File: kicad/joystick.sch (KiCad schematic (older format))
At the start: 16 parts, among them U13 74AHC541, U14 74AHC541

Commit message: Update to Kicad 5
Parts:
- C8, C9: symbol C -> Device:C
- JOY1, JOY2: symbol DB9_Male_MountingHoles -> Connector:DB9_Male_MountingHoles
- R10, R11, R2, R3, R4, R5, R6, R7, R8, R9: symbol R -> Device:R
- U13, U14: symbol 74LS541 -> 74xx:74LS541
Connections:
- wire segments 82 -> 102

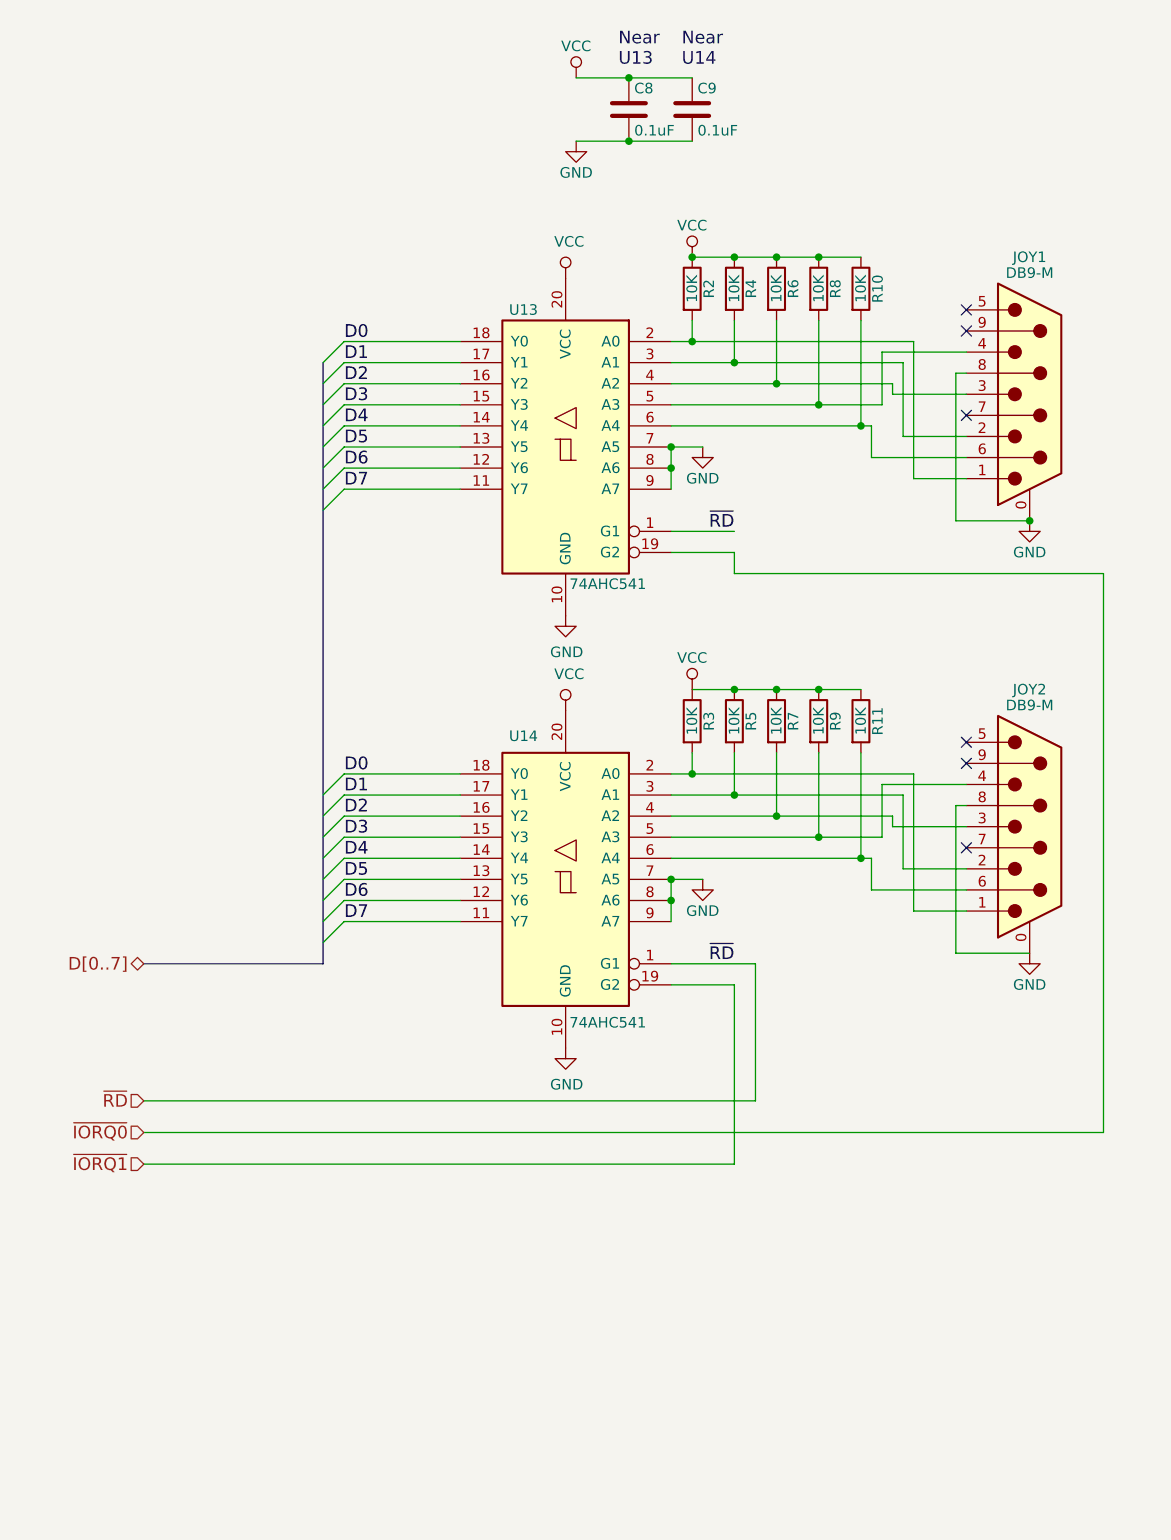
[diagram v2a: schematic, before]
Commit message: Hook up SD card slot's write protect and card detect lines.
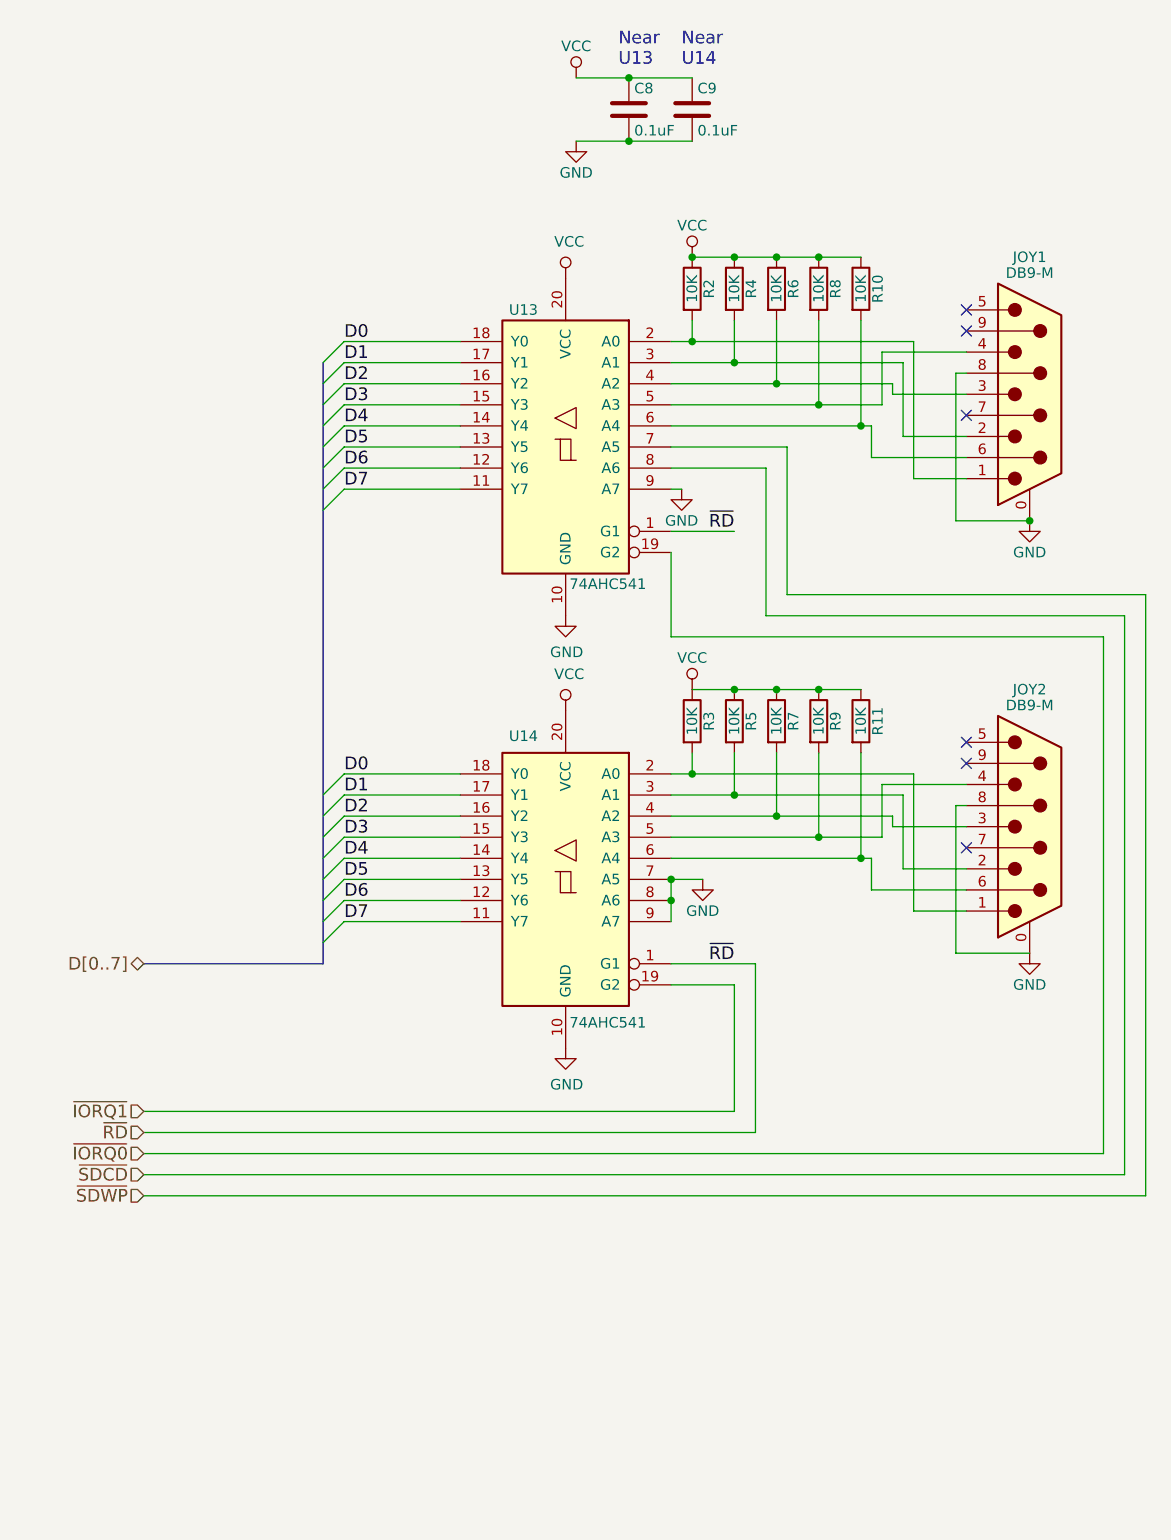
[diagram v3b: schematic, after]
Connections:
- net GND: no longer U13.7 (A5), U13.8 (A6)
- new net ~SDCD: U13.8 (A6)
- new net ~SDWP: U13.7 (A5)
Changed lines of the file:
@@
 Wire Wire Line
 	6250 2550 6250 2050
-Wire Wire Line
-	5350 3150 5650 3150
 $Comp
 L power:GND #PWR026
 U 1 1 59D6AB23
-P 5500 2650
-F 0 "#PWR026" H 5500 2400 50  0001 C CNN
-F 1 "GND" H 5500 2500 50  0000 C CNN
-F 2 "" H 5500 2650 50  0001 C CNN
-F 3 "" H 5500 2650 50  0001 C CNN
-	1    5500 2650
-	1    0    0    -1
-$EndComp
-Wire Wire Line
-	5350 2650 5500 2650
+P 5400 2850
+F 0 "#PWR026" H 5400 2600 50  0001 C CNN
+F 1 "GND" H 5400 2700 50  0000 C CNN
+F 2 "" H 5400 2850 50  0001 C CNN
+F 3 "" H 5400 2850 50  0001 C CNN
+	1    5400 2850
+	1    0    0    -1
+$EndComp
 Wire Wire Line
 	6750 2800 6500 2800
@@
 Text HLabel 2850 5100 0    60   BiDi ~ 0
 D[0..7]
-Text HLabel 2850 5750 0    60   Input ~ 0
+Text HLabel 2850 5900 0    60   Input ~ 0
 ~RD
 Wire Wire Line
-	2850 5750 5750 5750
-Text HLabel 2850 5900 0    60   Input ~ 0
+	2850 5900 5750 5900
+Text HLabel 2850 6000 0    60   Input ~ 0
 ~IORQ0
-Text HLabel 2850 6050 0    60   Input ~ 0
+Text HLabel 2850 5800 0    60   Input ~ 0
 ~IORQ1
 Wire Wire Line
-	5650 6050 2850 6050
-Wire Wire Line
-	2850 5900 7400 5900
-Wire Wire Line
-	7400 3250 5650 3250
-Wire Wire Line
-	5650 3250 5650 3150
+	5650 5800 2850 5800
 Wire Bus Line
 	3700 5100 2850 5100
@@
 	5150 1200 5450 1200
 Wire Wire Line
-	5350 2850 5350 2750
-Wire Wire Line
-	5350 2750 5350 2650
-Connection ~ 5350 2750
-Connection ~ 5350 2650
-Wire Wire Line
 	5350 4900 5350 4800
 Wire Wire Line
@@
 $EndComp
 Wire Wire Line
-	5750 5100 5750 5750
-Wire Wire Line
-	5650 5200 5650 6050
+	5750 5100 5750 5900
+Wire Wire Line
+	5650 5200 5650 5800
 Connection ~ 5450 1750
 Connection ~ 7050 3000
@@
 $EndComp
 Wire Wire Line
-	7400 3250 7400 5900
+	5400 2850 5350 2850
+Wire Wire Line
+	2850 6000 7400 6000
+Wire Wire Line
+	5350 3150 5350 3550
+Wire Wire Line
+	5350 3550 7400 3550
+Wire Wire Line
+	7400 3550 7400 6000
+Wire Wire Line
+	5350 2750 5800 2750
+Wire Wire Line
+	5800 2750 5800 3450
+Wire Wire Line
+	5800 3450 7500 3450
+Wire Wire Line
+	7500 3450 7500 6100
+Wire Wire Line
+	7500 6100 2850 6100
+Wire Wire Line
+	5350 2650 5900 2650
+Wire Wire Line
+	5900 2650 5900 3350
+Wire Wire Line
+	5900 3350 7600 3350
+Wire Wire Line
+	7600 3350 7600 6200
+Wire Wire Line
+	7600 6200 2850 6200
 Wire Bus Line
 	3700 2250 3700 5100
+Text HLabel 2850 6100 0    60   Input ~ 0
+~SDCD
+Text HLabel 2850 6200 0    60   Input ~ 0
+~SDWP
 $EndSCHEMATC

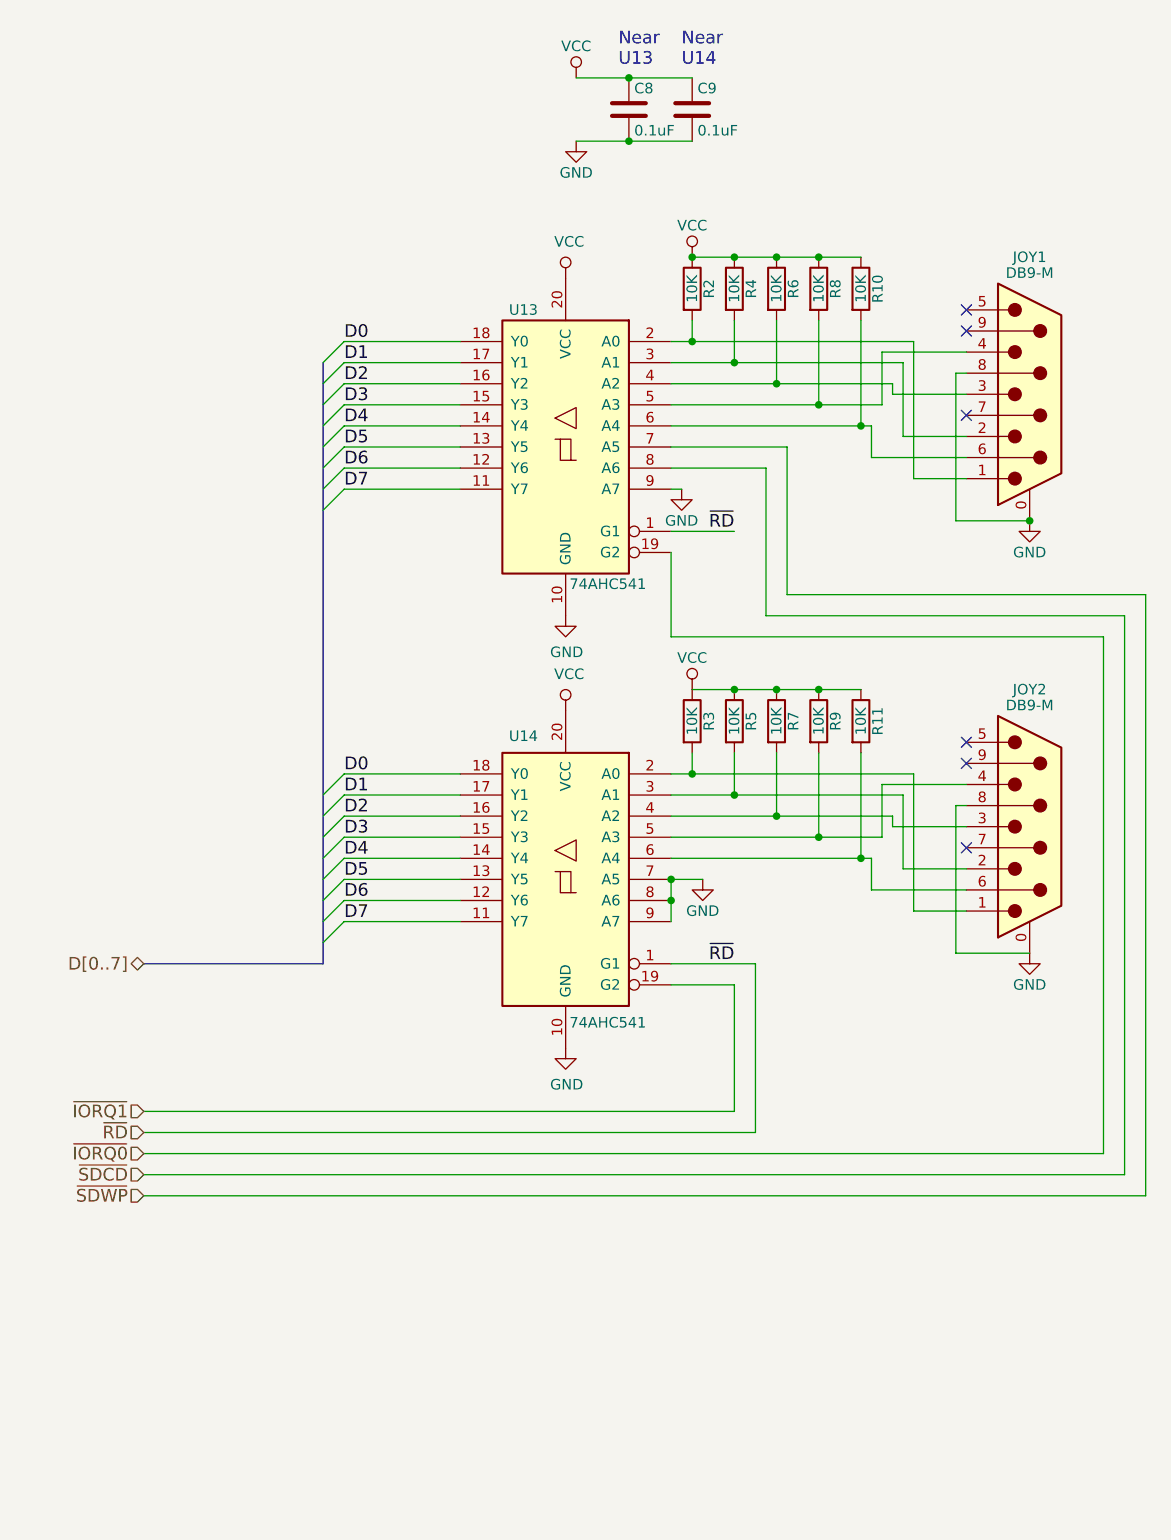
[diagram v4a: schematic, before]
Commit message: First complete version of ZED-80 schematic.
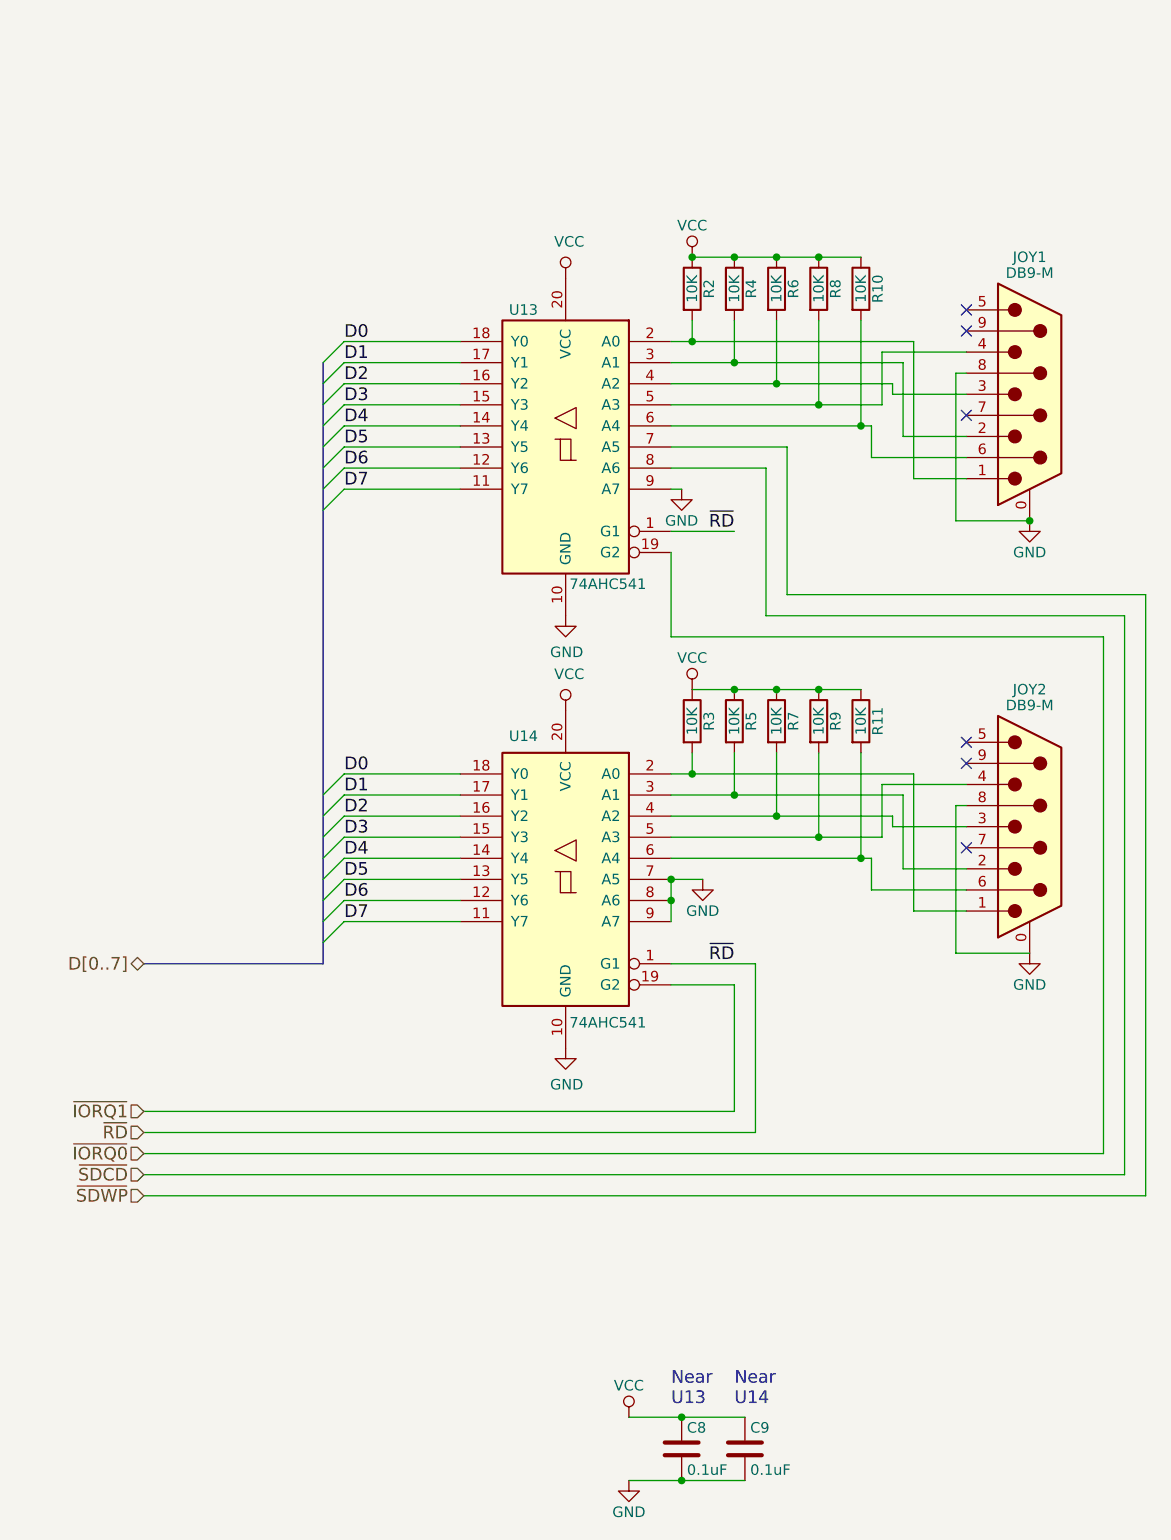
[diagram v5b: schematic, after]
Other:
- moved on the sheet: C8, C9
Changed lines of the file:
@@
 EESchema Schematic File Version 4
-LIBS:z80-cache
 EELAYER 29 0
 EELAYER END
@@
 Sheet 2 11
 Title "Joystick Ports"
-Date "2018-07-20"
-Rev "12"
+Date "2019-04-03"
+Rev "1"
 Comp ""
 Comment1 ""
@@
 L Device:C C8
 U 1 1 59D817E3
-P 5150 1050
-F 0 "C8" H 5175 1150 50  0000 L CNN
-F 1 "0.1uF" H 5175 950 50  0000 L CNN
-F 2 "Capacitors_THT:C_Disc_D4.3mm_W1.9mm_P5.00mm" H 5188 900 50  0001 C CNN
-F 3 "" H 5150 1050 50  0001 C CNN
-	1    5150 1050
+P 5400 7400
+F 0 "C8" H 5425 7500 50  0000 L CNN
+F 1 "0.1uF" H 5425 7300 50  0000 L CNN
+F 2 "Capacitors_THT:C_Disc_D4.3mm_W1.9mm_P5.00mm" H 5438 7250 50  0001 C CNN
+F 3 "" H 5400 7400 50  0001 C CNN
+	1    5400 7400
 	1    0    0    -1
 $EndComp
@@
 L power:GND #PWR030
 U 1 1 59D817EA
-P 4900 1200
-F 0 "#PWR030" H 4900 950 50  0001 C CNN
-F 1 "GND" H 4900 1050 50  0000 C CNN
-F 2 "" H 4900 1200 50  0001 C CNN
-F 3 "" H 4900 1200 50  0001 C CNN
-	1    4900 1200
+P 5150 7550
+F 0 "#PWR030" H 5150 7300 50  0001 C CNN
+F 1 "GND" H 5150 7400 50  0000 C CNN
+F 2 "" H 5150 7550 50  0001 C CNN
+F 3 "" H 5150 7550 50  0001 C CNN
+	1    5150 7550
 	1    0    0    -1
 $EndComp
@@
 L Device:C C9
 U 1 1 59D817F0
-P 5450 1050
-F 0 "C9" H 5475 1150 50  0000 L CNN
-F 1 "0.1uF" H 5475 950 50  0000 L CNN
-F 2 "Capacitors_THT:C_Disc_D4.3mm_W1.9mm_P5.00mm" H 5488 900 50  0001 C CNN
-F 3 "" H 5450 1050 50  0001 C CNN
-	1    5450 1050
+P 5700 7400
+F 0 "C9" H 5725 7500 50  0000 L CNN
+F 1 "0.1uF" H 5725 7300 50  0000 L CNN
+F 2 "Capacitors_THT:C_Disc_D4.3mm_W1.9mm_P5.00mm" H 5738 7250 50  0001 C CNN
+F 3 "" H 5700 7400 50  0001 C CNN
+	1    5700 7400
 	1    0    0    -1
 $EndComp
@@
 L power:VCC #PWR031
 U 1 1 59D817F7
-P 4900 900
-F 0 "#PWR031" H 4900 750 50  0001 C CNN
-F 1 "VCC" H 4900 1050 50  0000 C CNN
-F 2 "" H 4900 900 50  0001 C CNN
-F 3 "" H 4900 900 50  0001 C CNN
-	1    4900 900
-	1    0    0    -1
-$EndComp
-Text Notes 5100 850  0    60   ~ 0
+P 5150 7250
+F 0 "#PWR031" H 5150 7100 50  0001 C CNN
+F 1 "VCC" H 5150 7400 50  0000 C CNN
+F 2 "" H 5150 7250 50  0001 C CNN
+F 3 "" H 5150 7250 50  0001 C CNN
+	1    5150 7250
+	1    0    0    -1
+$EndComp
+Text Notes 5350 7200 0    60   ~ 0
 Near\nU13
-Text Notes 5400 850  0    60   ~ 0
+Text Notes 5650 7200 0    60   ~ 0
 Near\nU14
-Connection ~ 5150 900
-Connection ~ 5150 1200
-Wire Wire Line
-	4900 1200 5150 1200
-Wire Wire Line
-	4900 900  5150 900
+Connection ~ 5400 7250
+Connection ~ 5400 7550
+Wire Wire Line
+	5150 7550 5400 7550
+Wire Wire Line
+	5150 7250 5400 7250
 Wire Wire Line
 	6050 1750 6250 1750
@@
 	6050 3800 6250 3800
 Wire Wire Line
-	5150 900  5450 900
-Wire Wire Line
-	5150 1200 5450 1200
+	5400 7250 5700 7250
+Wire Wire Line
+	5400 7550 5700 7550
 Wire Wire Line
 	5350 4900 5350 4800
